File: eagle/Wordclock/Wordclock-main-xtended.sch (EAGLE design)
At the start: 59 parts, among them IC1 MEGA8-P, J1 AVR_SPI_PRG_6PTH, Q1 16MHz, T1 EBC pinout

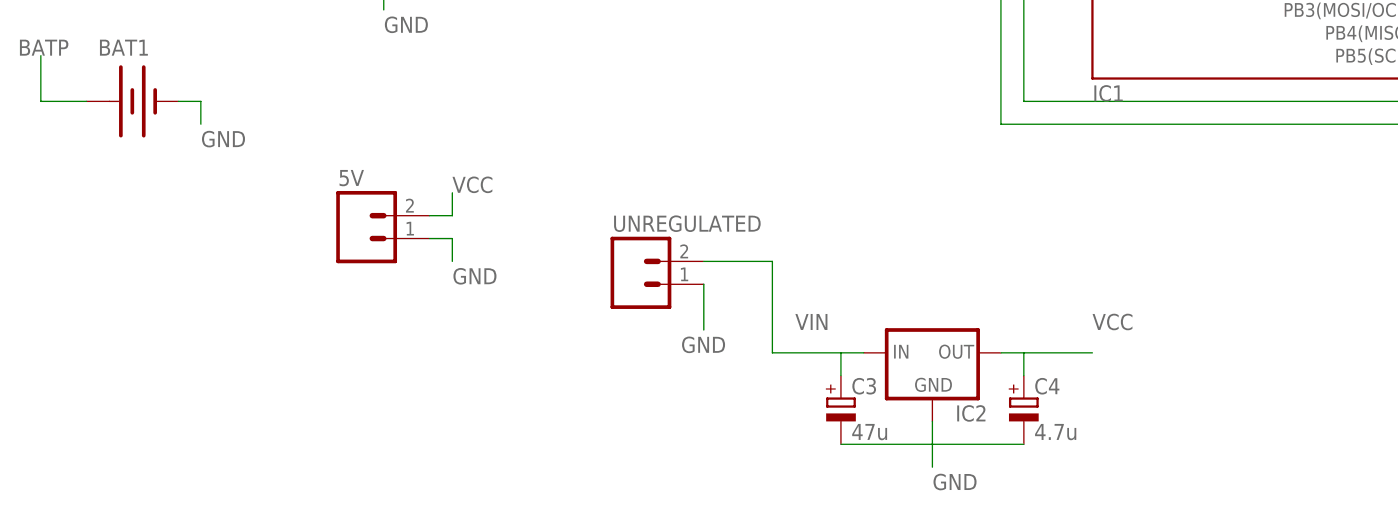
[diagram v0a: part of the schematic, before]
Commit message: Worclock extended version wired beta, wired. Todo verify before production.
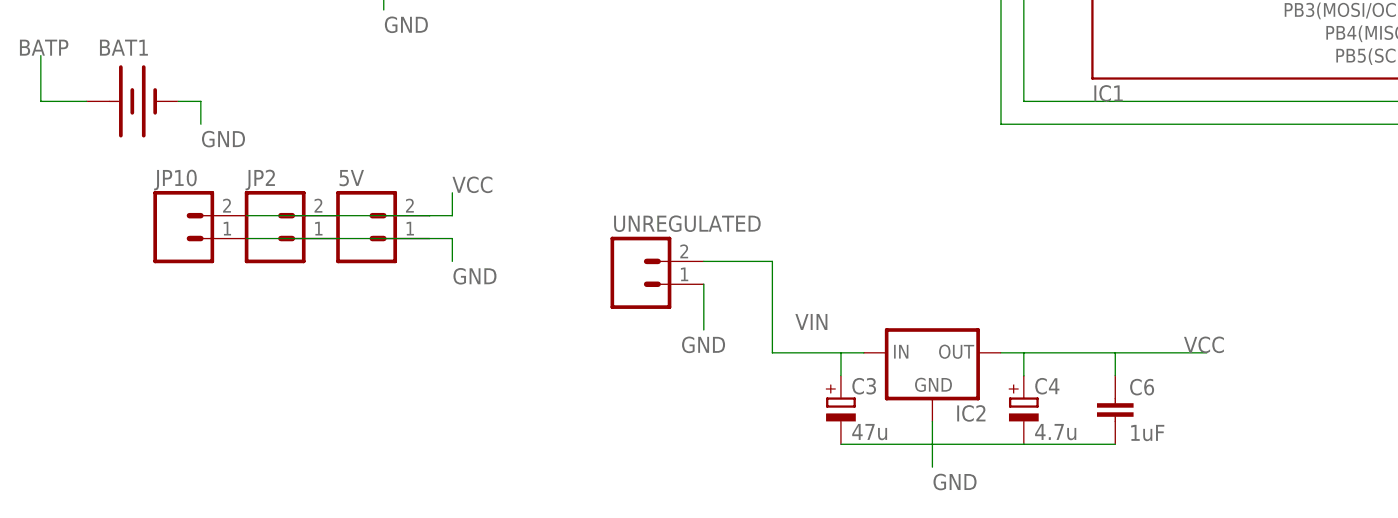
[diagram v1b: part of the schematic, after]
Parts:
- added C6: 1uF, resistor:C-EU025-024X044
- added JP10, JP2: (no value), SparkFun-Connectors:M02PTH3
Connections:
- net GND: now also C6.2, JP10.1, JP2.1
- net VCC: now also C6.1, JP10.2, JP2.2
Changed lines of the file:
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@@
 <part name="U$9" library="kalshagar" deviceset="M7_NOSILK" device=""/>
 <part name="U$10" library="kalshagar" deviceset="M7_NOSILK" device=""/>
+<part name="C6" library="resistor" deviceset="C-EU" device="025-024X044" value="1uF"/>
+<part name="JP2" library="SparkFun-Connectors" deviceset="M02" device="PTH3"/>
+<part name="JP10" library="SparkFun-Connectors" deviceset="M02" device="PTH3"/>
 </parts>
 <sheets>
@@
 <instance part="U$9" gate="G$1" x="210.82" y="121.92"/>
 <instance part="U$10" gate="G$1" x="203.2" y="121.92"/>
+<instance part="C6" gate="G$1" x="43.18" y="-12.7"/>
+<instance part="JP2" gate="G$1" x="-50.8" y="5.08"/>
+<instance part="JP10" gate="G$1" x="-60.96" y="5.08"/>
 </instances>
 <busses>
@@
 <wire x1="-30.48" y1="5.08" x2="-30.48" y2="2.54" width="0.1524" layer="91"/>
 <label x="-30.48" y="0" size="1.778" layer="95"/>
+<pinref part="JP10" gate="G$1" pin="1"/>
+<pinref part="JP2" gate="G$1" pin="1"/>
+<wire x1="-53.34" y1="5.08" x2="-43.18" y2="5.08" width="0.1524" layer="91"/>
+<wire x1="-43.18" y1="5.08" x2="-33.02" y2="5.08" width="0.1524" layer="91"/>
 </segment>
 <segment>
@@
 <wire x1="22.86" y1="-17.78" x2="22.86" y2="-20.32" width="0.1524" layer="91"/>
 <label x="22.86" y="-22.86" size="1.778" layer="95"/>
+<pinref part="C6" gate="G$1" pin="2"/>
+<wire x1="43.18" y1="-17.78" x2="33.02" y2="-17.78" width="0.1524" layer="91"/>
 </segment>
 <segment>
@@
 <wire x1="-30.48" y1="7.62" x2="-30.48" y2="10.16" width="0.1524" layer="91"/>
 <label x="-30.48" y="10.16" size="1.778" layer="95"/>
+<pinref part="JP10" gate="G$1" pin="2"/>
+<pinref part="JP2" gate="G$1" pin="2"/>
+<wire x1="-53.34" y1="7.62" x2="-43.18" y2="7.62" width="0.1524" layer="91"/>
+<wire x1="-43.18" y1="7.62" x2="-33.02" y2="7.62" width="0.1524" layer="91"/>
 </segment>
 <segment>
@@
 <wire x1="30.48" y1="-7.62" x2="33.02" y2="-7.62" width="0.1524" layer="91"/>
 <pinref part="C4" gate="G$1" pin="+"/>
-<wire x1="33.02" y1="-7.62" x2="40.64" y2="-7.62" width="0.1524" layer="91"/>
+<wire x1="33.02" y1="-7.62" x2="43.18" y2="-7.62" width="0.1524" layer="91"/>
+<wire x1="43.18" y1="-7.62" x2="53.34" y2="-7.62" width="0.1524" layer="91"/>
 <wire x1="33.02" y1="-10.16" x2="33.02" y2="-7.62" width="0.1524" layer="91"/>
-<label x="40.64" y="-5.08" size="1.778" layer="95"/>
-</segment>
-<segment>
+<label x="50.8" y="-7.62" size="1.778" layer="95"/>
+<pinref part="C6" gate="G$1" pin="1"/>
+<wire x1="43.18" y1="-10.16" x2="43.18" y2="-7.62" width="0.1524" layer="91"/>
+</segment>
+<segment>

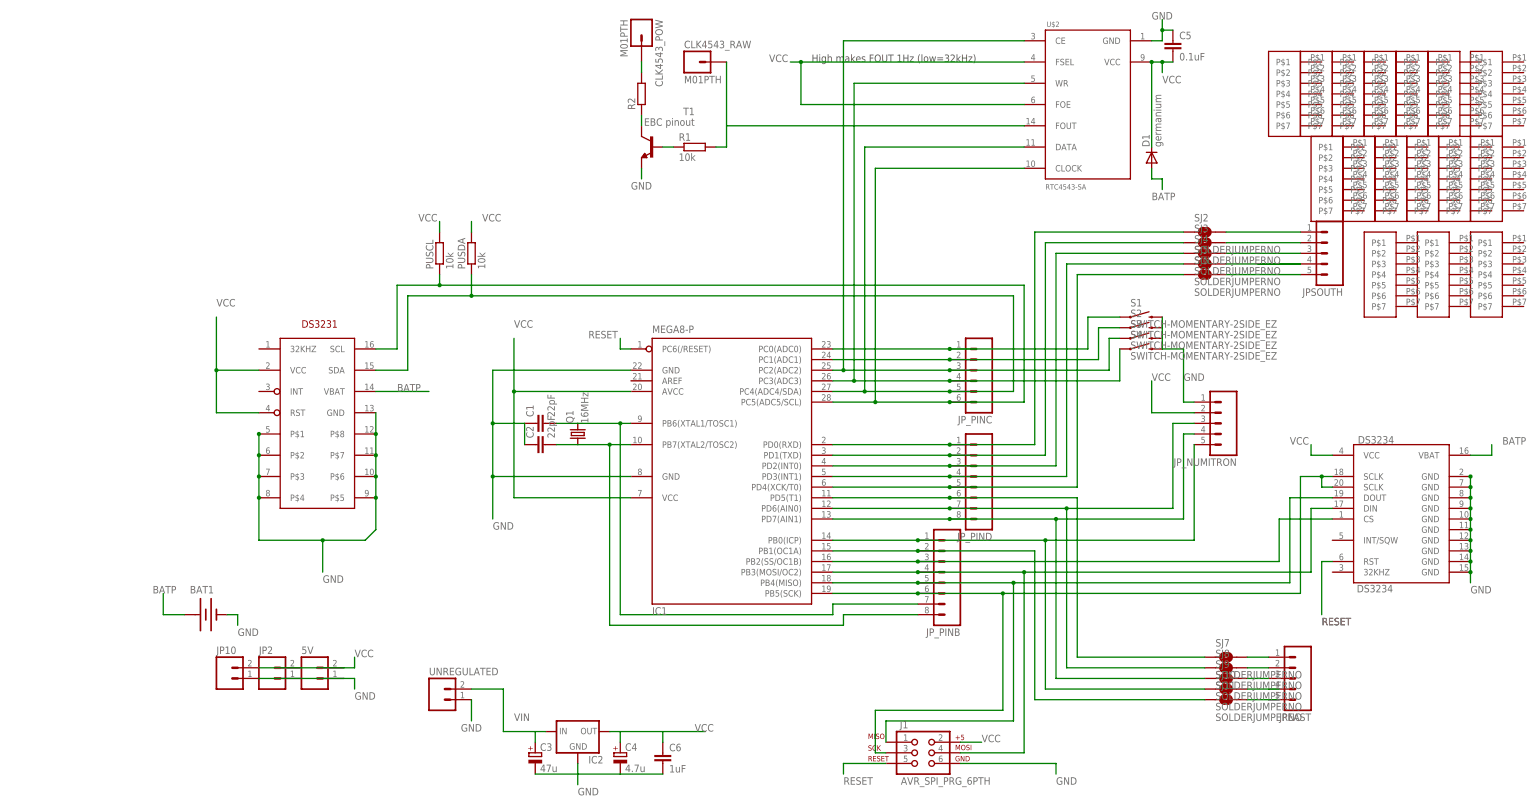
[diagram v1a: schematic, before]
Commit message: Started adding the labels
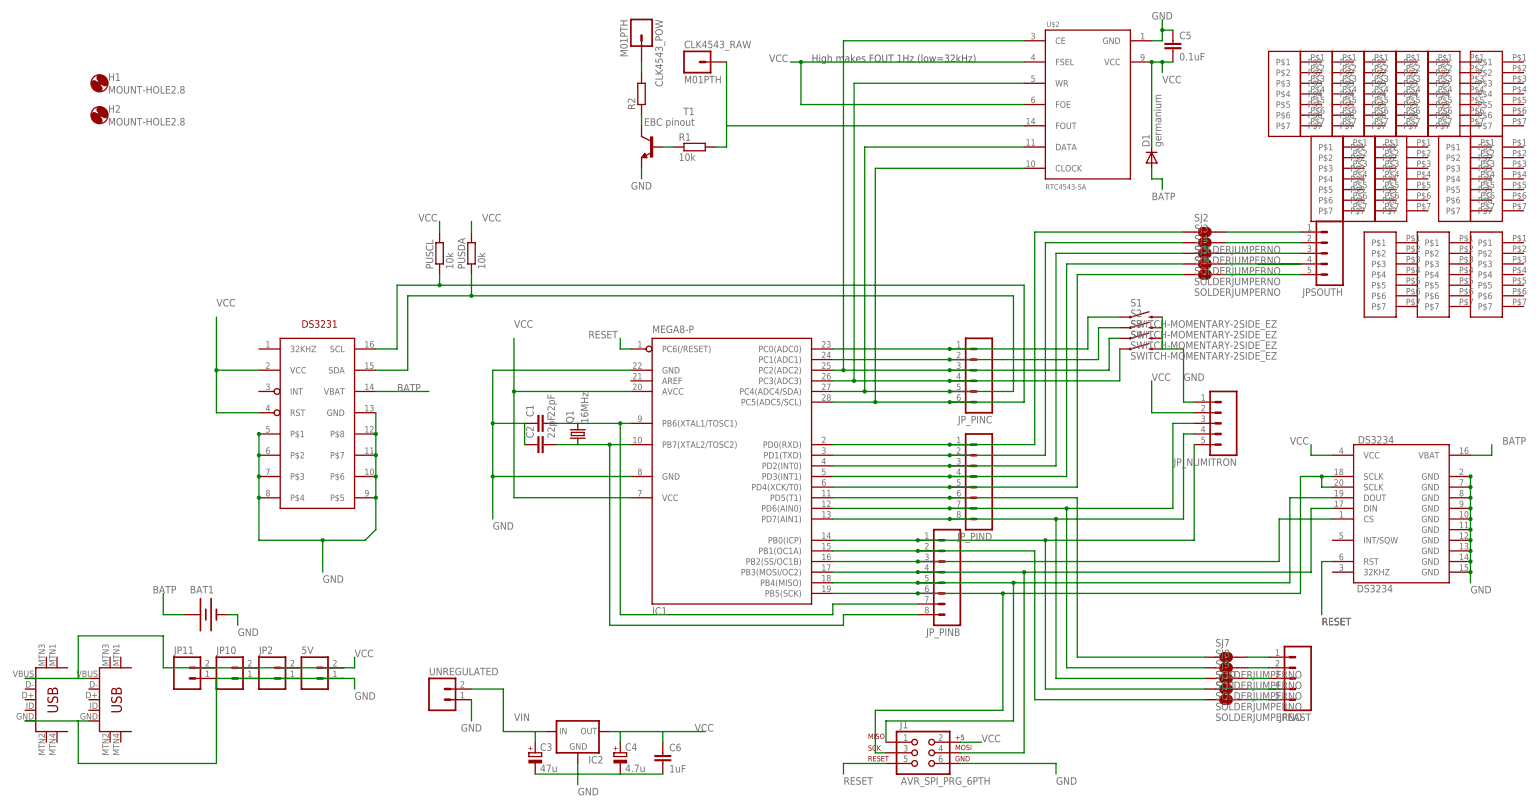
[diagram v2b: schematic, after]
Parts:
- removed U$7: M7_NOSILK, kalshagar:M7_NOSILK
- added H1, H2: MOUNT-HOLE2.8, holes:MOUNT-HOLE2.8
- added JP11: (no value), SparkFun-Connectors:M02PTH3
- added U$11, U$12: USB-MINIB-5PIN, SparkFun-Connectors:USB-MINIB-5PIN
- 5V: device SparkFun:M02PTH3 -> SparkFun-Connectors:M02PTH
- JP2: device SparkFun-Connectors:M02PTH3 -> SparkFun-Connectors:M02PTH
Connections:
- net GND: now also JP11.1, U$11.GND, U$12.GND
- net VCC: now also JP11.2, U$11.VBUS, U$12.VBUS
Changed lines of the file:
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@@
 <part name="IC1" library="atmel" deviceset="MEGA8-P" device=""/>
 <part name="U$1" library="kalshagar" deviceset="DS3231" device="DS3231-SO16W"/>
-<part name="5V" library="SparkFun" deviceset="M02" device="PTH3"/>
+<part name="5V" library="SparkFun-Connectors" deviceset="M02" device="PTH"/>
 <part name="PUSCL" library="resistor" deviceset="R-EU_" device="0204/5" value="10k"/>
 <part name="PUSDA" library="resistor" deviceset="R-EU_" device="0204/5" value="10k"/>
@@
 <part name="U$5" library="kalshagar" deviceset="M7_NOSILK" device=""/>
 <part name="U$6" library="kalshagar" deviceset="M7_NOSILK" device=""/>
-<part name="U$7" library="kalshagar" deviceset="M7_NOSILK" device=""/>
 <part name="U$8" library="kalshagar" deviceset="M7_NOSILK" device=""/>
 <part name="U$9" library="kalshagar" deviceset="M7_NOSILK" device=""/>
 <part name="U$10" library="kalshagar" deviceset="M7_NOSILK" device=""/>
 <part name="C6" library="resistor" deviceset="C-EU" device="025-024X044" value="1uF"/>
-<part name="JP2" library="SparkFun-Connectors" deviceset="M02" device="PTH3"/>
+<part name="JP2" library="SparkFun-Connectors" deviceset="M02" device="PTH"/>
 <part name="JP10" library="SparkFun-Connectors" deviceset="M02" device="PTH3"/>
+<part name="JP11" library="SparkFun-Connectors" deviceset="M02" device="PTH3"/>
+<part name="U$11" library="SparkFun-Connectors" deviceset="USB-MINIB" device="-5PIN"/>
+<part name="U$12" library="SparkFun-Connectors" deviceset="USB-MINIB" device="-5PIN"/>
+<part name="H1" library="holes" deviceset="MOUNT-HOLE" device="2.8"/>
+<part name="H2" library="holes" deviceset="MOUNT-HOLE" device="2.8"/>
 </parts>
 <sheets>
@@
 <instance part="U$5" gate="G$1" x="241.3" y="121.92"/>
 <instance part="U$6" gate="G$1" x="233.68" y="121.92"/>
-<instance part="U$7" gate="G$1" x="226.06" y="121.92"/>
 <instance part="U$8" gate="G$1" x="218.44" y="121.92"/>
 <instance part="U$9" gate="G$1" x="210.82" y="121.92"/>
@@
 <instance part="JP2" gate="G$1" x="-50.8" y="5.08"/>
 <instance part="JP10" gate="G$1" x="-60.96" y="5.08"/>
+<instance part="JP11" gate="G$1" x="-71.12" y="5.08"/>
+<instance part="U$11" gate="G$1" x="-91.44" y="-5.08"/>
+<instance part="U$12" gate="G$1" x="-106.68" y="-5.08"/>
+<instance part="H1" gate="G$1" x="-91.44" y="147.32"/>
+<instance part="H2" gate="G$1" x="-91.44" y="139.7"/>
 </instances>
 <busses>
@@
 <wire x1="-53.34" y1="5.08" x2="-43.18" y2="5.08" width="0.1524" layer="91"/>
 <wire x1="-43.18" y1="5.08" x2="-33.02" y2="5.08" width="0.1524" layer="91"/>
+<pinref part="JP11" gate="G$1" pin="1"/>
+<wire x1="-63.5" y1="5.08" x2="-53.34" y2="5.08" width="0.1524" layer="91"/>
+<pinref part="U$11" gate="G$1" pin="GND"/>
+<wire x1="-93.98" y1="-5.08" x2="-96.52" y2="-5.08" width="0.1524" layer="91"/>
+<wire x1="-96.52" y1="-5.08" x2="-96.52" y2="-15.24" width="0.1524" layer="91"/>
+<wire x1="-96.52" y1="-15.24" x2="-63.5" y2="-15.24" width="0.1524" layer="91"/>
+<wire x1="-63.5" y1="-15.24" x2="-63.5" y2="5.08" width="0.1524" layer="91"/>
+<pinref part="U$12" gate="G$1" pin="GND"/>
+<wire x1="-109.22" y1="-5.08" x2="-96.52" y2="-5.08" width="0.1524" layer="91"/>
 </segment>
 <segment>
@@
 <wire x1="-53.34" y1="7.62" x2="-43.18" y2="7.62" width="0.1524" layer="91"/>
 <wire x1="-43.18" y1="7.62" x2="-33.02" y2="7.62" width="0.1524" layer="91"/>
-</segment>
-<segment>
+<pinref part="JP11" gate="G$1" pin="2"/>
+<wire x1="-63.5" y1="7.62" x2="-53.34" y2="7.62" width="0.1524" layer="91"/>
+<pinref part="U$11" gate="G$1" pin="VBUS"/>
+<wire x1="-93.98" y1="5.08" x2="-96.52" y2="5.08" width="0.1524" layer="91"/>
+<wire x1="-96.52" y1="5.08" x2="-96.52" y2="15.24" width="0.1524" layer="91"/>
+<wire x1="-96.52" y1="15.24" x2="-76.2" y2="15.24" width="0.1524" layer="91"/>
+<wire x1="-76.2" y1="15.24" x2="-76.2" y2="7.62" width="0.1524" layer="91"/>
+<wire x1="-76.2" y1="7.62" x2="-63.5" y2="7.62" width="0.1524" layer="91"/>
+<pinref part="U$12" gate="G$1" pin="VBUS"/>
+<wire x1="-109.22" y1="5.08" x2="-96.52" y2="5.08" width="0.1524" layer="91"/>
+</segment>
+<segment>

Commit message: Added labels, need a final review and go to production.
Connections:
- net GND: now also U$8.P$1, U$8.P$2, U$8.P$3, U$8.P$4
- net VCC: now also U$10.P$1, U$8.P$5, U$8.P$6, U$8.P$7
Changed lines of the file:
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@@
 <instance part="U$8" gate="G$1" x="218.44" y="121.92"/>
 <instance part="U$9" gate="G$1" x="210.82" y="121.92"/>
-<instance part="U$10" gate="G$1" x="203.2" y="121.92"/>
+<instance part="U$10" gate="G$1" x="190.5" y="121.92"/>
 <instance part="C6" gate="G$1" x="43.18" y="-12.7"/>
 <instance part="JP2" gate="G$1" x="-50.8" y="5.08"/>
@@
 <label x="35.56" y="121.92" size="1.778" layer="95"/>
 </segment>
+<segment>
+<pinref part="U$8" gate="G$1" pin="P$1"/>
+<pinref part="U$8" gate="G$1" pin="P$2"/>
+<wire x1="226.06" y1="132.08" x2="226.06" y2="129.54" width="0.1524" layer="91"/>
+<pinref part="U$8" gate="G$1" pin="P$3"/>
+<wire x1="226.06" y1="129.54" x2="226.06" y2="127" width="0.1524" layer="91"/>
+<pinref part="U$8" gate="G$1" pin="P$4"/>
+<wire x1="226.06" y1="127" x2="226.06" y2="124.46" width="0.1524" layer="91"/>
+</segment>
 </net>
 <net name="N$30" class="0">
@@
 <wire x1="76.2" y1="142.24" x2="76.2" y2="152.4" width="0.1524" layer="91"/>
 </segment>
-</net>
+<segment>
+<pinref part="U$8" gate="G$1" pin="P$5"/>
+<pinref part="U$8" gate="G$1" pin="P$6"/>
+<wire x1="226.06" y1="121.92" x2="226.06" y2="119.38" width="0.1524" layer="91"/>
+<pinref part="U$8" gate="G$1" pin="P$7"/>
+<wire x1="226.06" y1="119.38" x2="226.06" y2="116.84" width="0.1524" layer="91"/>
+</segment>
+<segment>
+<pinref part="U$10" gate="G$1" pin="P$1"/>
+<wire x1="198.12" y1="132.08" x2="200.66" y2="132.08" width="0.1524" layer="91"/>
+</segment>
+</net>
